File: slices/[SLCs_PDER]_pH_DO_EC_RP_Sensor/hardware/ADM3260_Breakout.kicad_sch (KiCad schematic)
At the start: 21 parts, among them J1 CONN_05LOCK_LONGPADS, J2 BNCPTH, Q1 BSS84, Q2 BSH105, Q3 BSS84, U1 ADM3260, U2 Atlas Scientific OEM pH or ORP

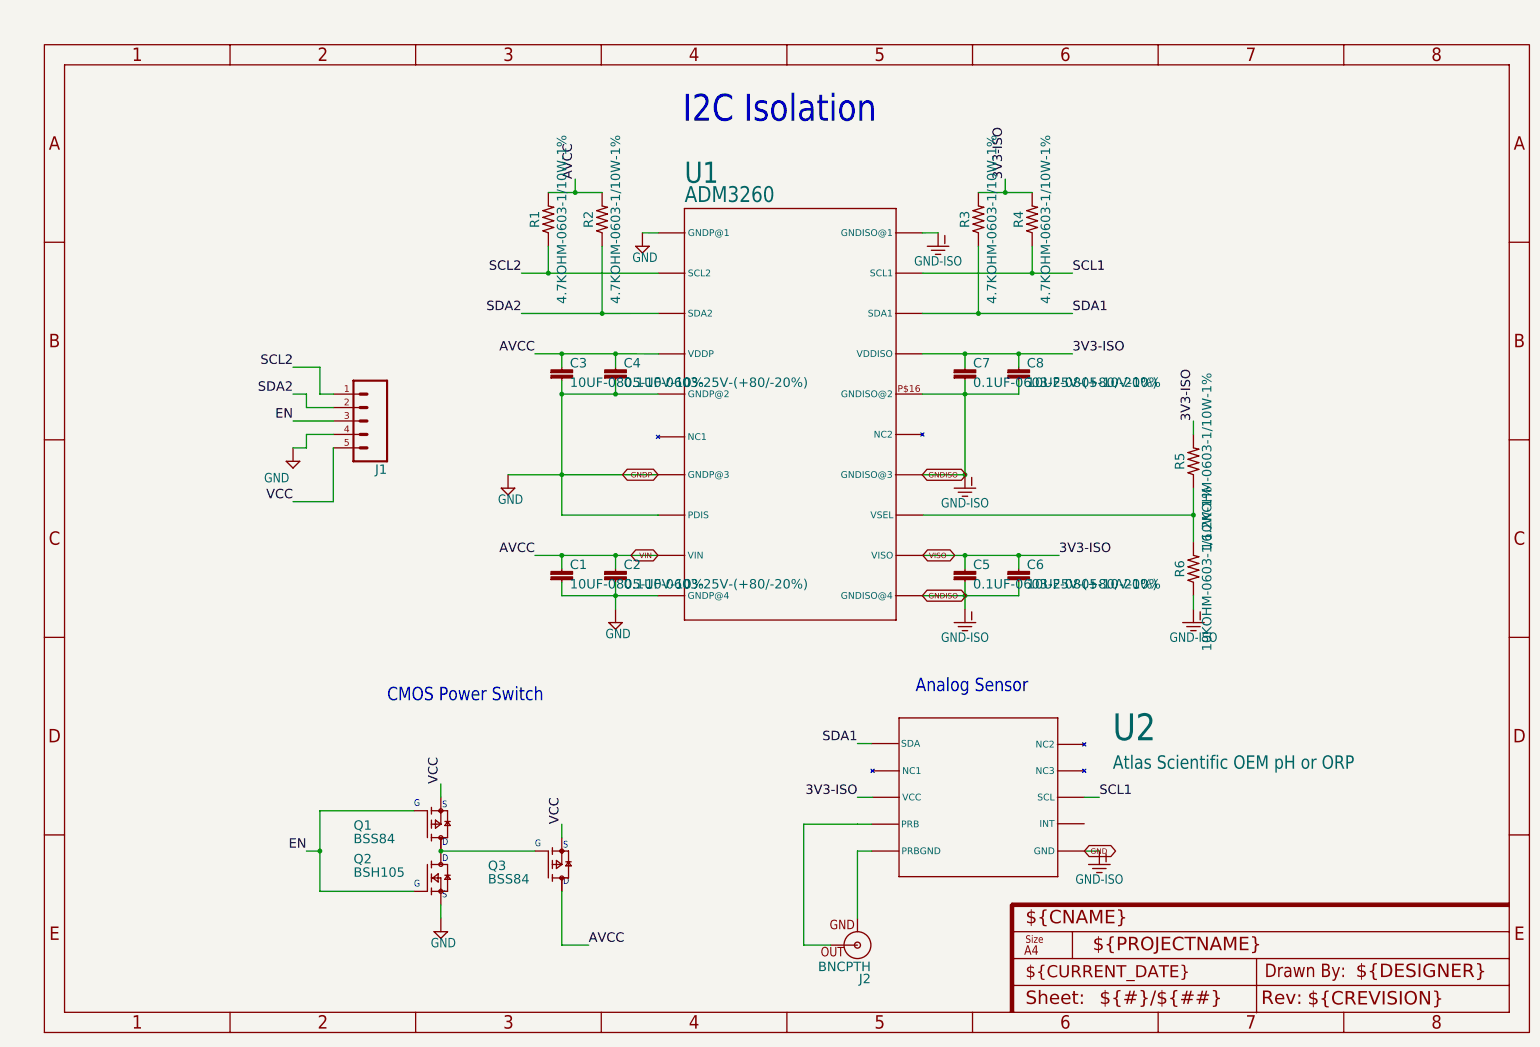
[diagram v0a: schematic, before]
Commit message: improved phdo and initial ERC pass on PDER
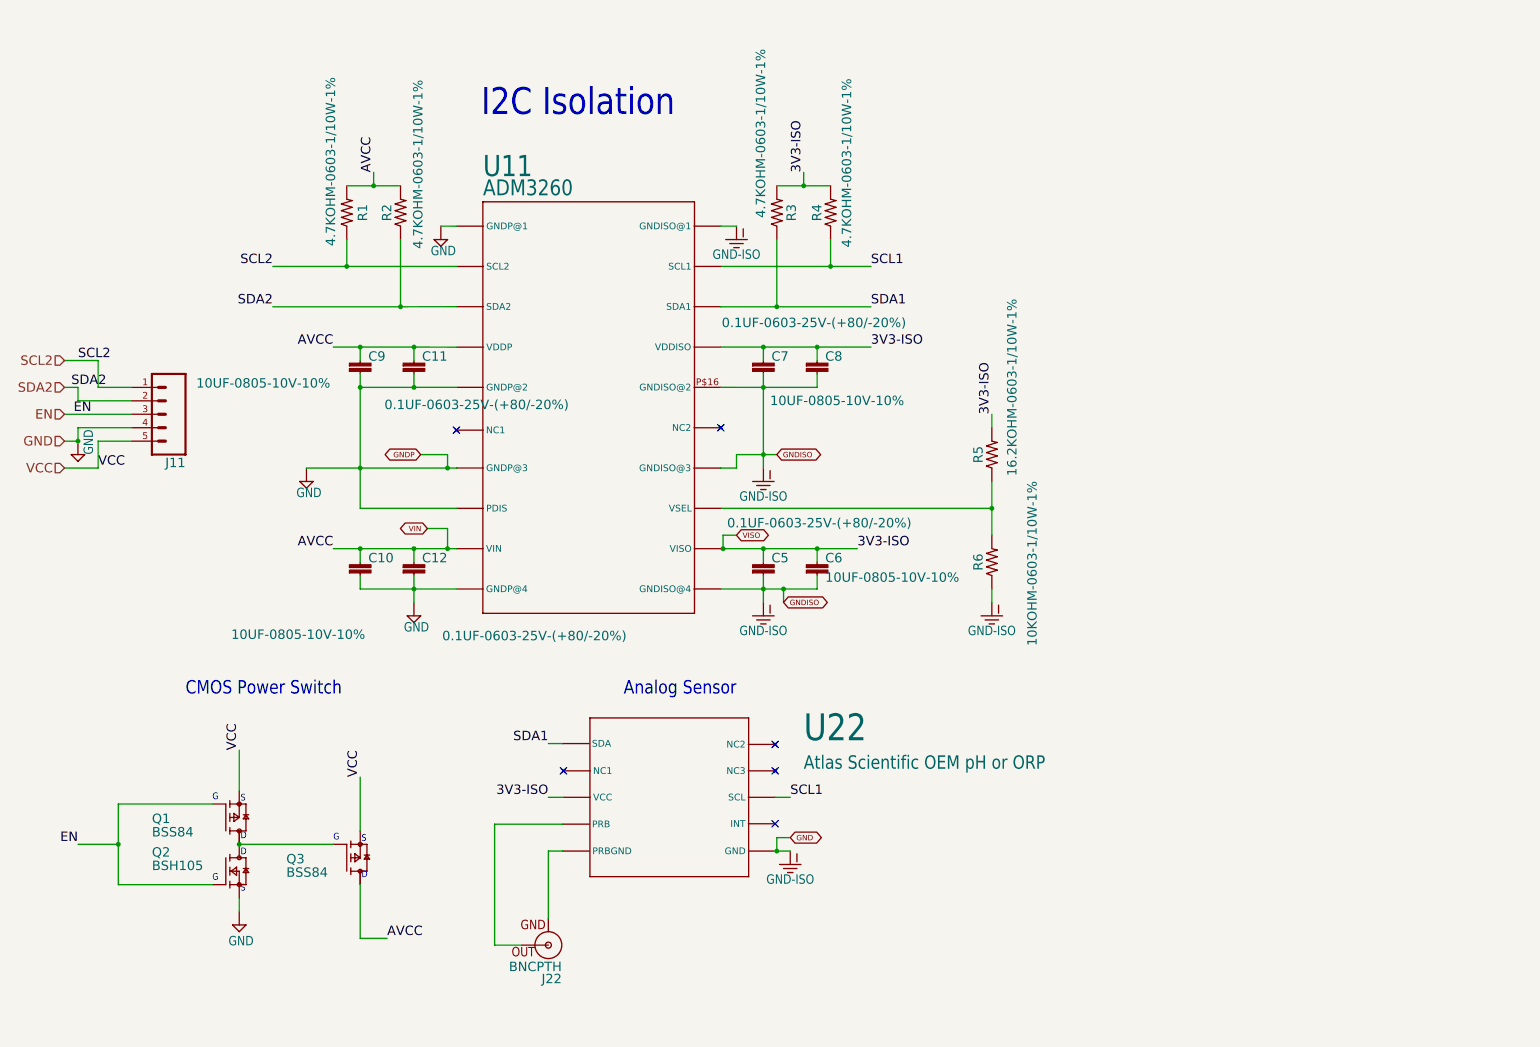
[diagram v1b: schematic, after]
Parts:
- C10: renamed from C1; footprint ADM3260_Breakout:0805 -> Capacitor_SMD:C_0805_2012Metric
- C11: renamed from C4; footprint ADM3260_Breakout:0603 -> Capacitor_SMD:C_0201_0603Metric
- C12: renamed from C2; footprint ADM3260_Breakout:0603 -> Capacitor_SMD:C_0201_0603Metric
- C5, C7: footprint ADM3260_Breakout:0603 -> Capacitor_SMD:C_0201_0603Metric
- C6, C8: footprint ADM3260_Breakout:0805 -> Capacitor_SMD:C_0805_2012Metric
- C9: renamed from C3; footprint ADM3260_Breakout:0805 -> Capacitor_SMD:C_0805_2012Metric
- J11: renamed from J1; footprint ADM3260_Breakout:1X05_LOCK_LONGPADS -> Connector_JST:JST_EH_B5B-EH-A_1x05_P2.50mm_Vertical
- J22: renamed from J2; footprint ADM3260_Breakout:BNC -> Connector_Coaxial:BNC_Amphenol_B6252HB-NPP3G-50_Horizontal
- Q1, Q2, Q3: footprint ADM3260_Breakout:SOT23 -> Package_TO_SOT_SMD:SOT-23-3
- R1, R2, R3, R4, R5, R6: footprint ADM3260_Breakout:0603 -> Resistor_SMD:R_0201_0603Metric
- renumbered U1 to U11, U2 to U22
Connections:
- net 3V3-ISO is gone; now on net VISO: C5.1, C6.1, C7.1, C8.1, R3.2, R4.2, R5.2, U11.P$17 (VDDISO), U22.P$3 (VCC)
- net AVCC is gone; now on net VIN: C10.1, C11.1, C12.1, C9.1, Q3.3 (D), R1.2, R2.2, U11.P$4 (VDDP)
- net GNDP is gone; now on net GND: U11.P$7 (GNDP@3)
- net GND: now also U11.P$8 (PDIS)
- net SDA1: now also U22.P$1 (SDA)
- net at J22.GND: now also U22.P$5 (PRBGND)
- net at J22.S (OUT): now also U22.P$4 (PRB)
- net at R5.1, R6.2: now also U11.P$13 (VSEL)
- no-connect marks 0 -> 6
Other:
- company: (none) -> FAST Research et al.
- title: (none) -> ADM3260 with Atlas Scientific OEM
- moved on the sheet: C10, C11, C12, C5, C6, C7, C8, C9, J11, J22, Q1, Q2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

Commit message: atlas oem slice footprints all done and at routing stage
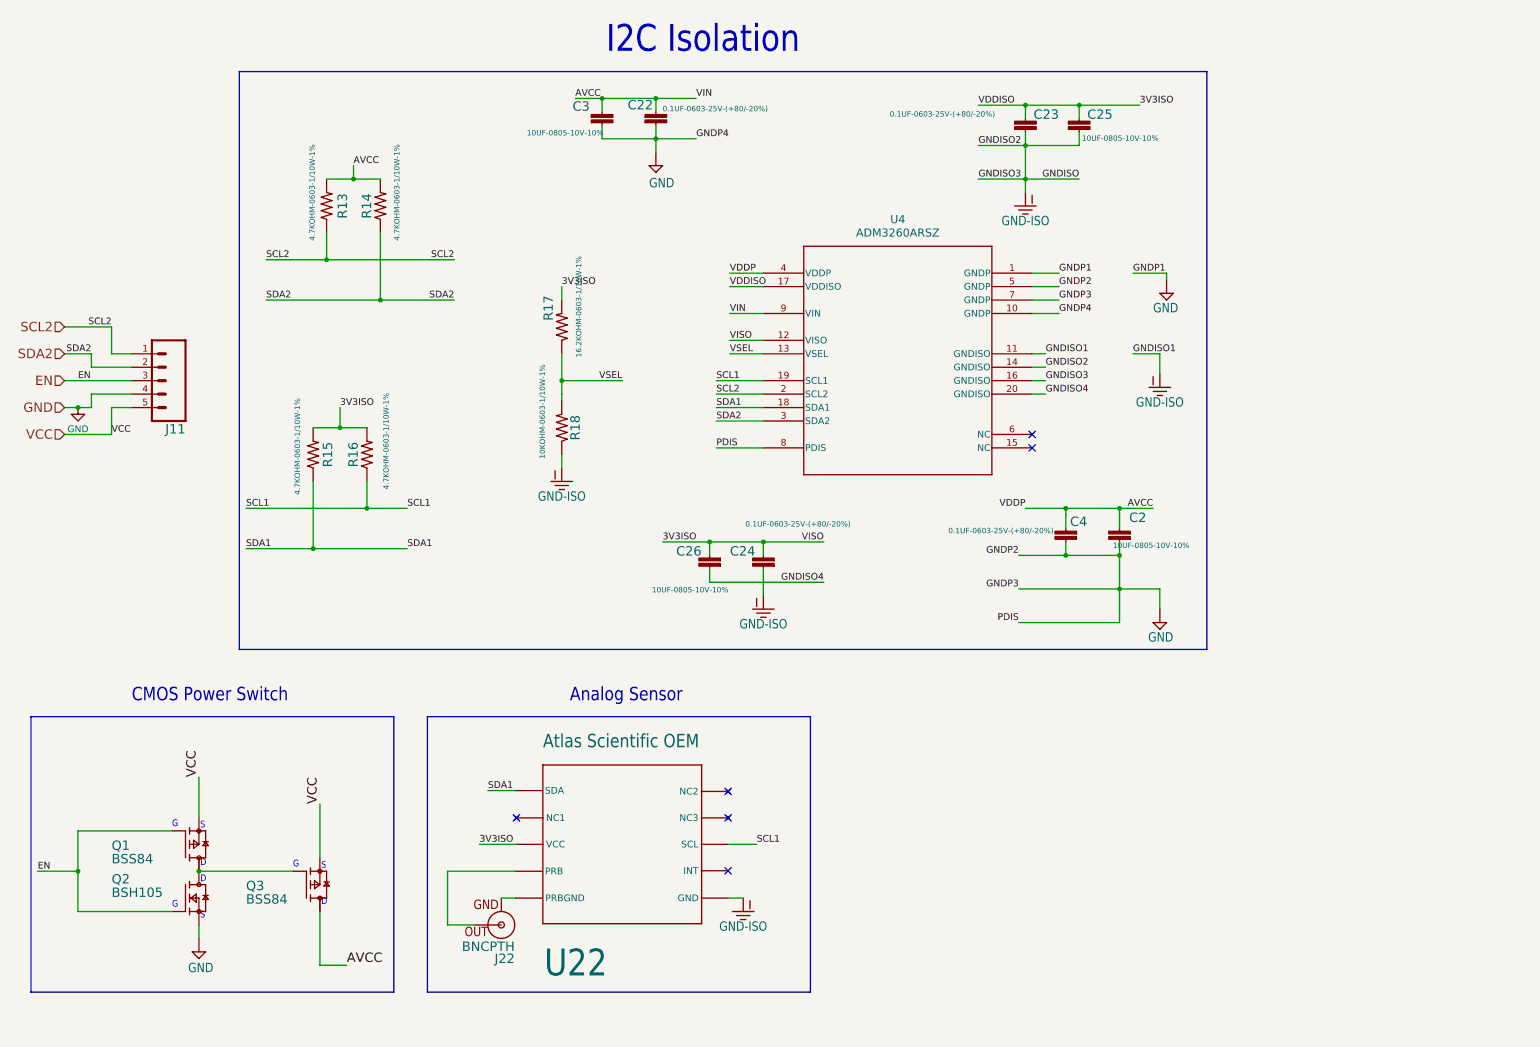
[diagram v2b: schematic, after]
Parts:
- removed C10, C6, C8, C9: 10UF-0805-10V-10%, Capacitor_SMD:C_0805_2012Metric, symbol ADM3260_Breakout-eagle-import:10UF-0805-10V-10%
- removed C11, C12, C5, C7: 0.1UF-0603-25V-(+80/-20%), Capacitor_SMD:C_0201_0603Metric, symbol ADM3260_Breakout-eagle-import:0.1UF-0603-25V-(+80/-20%)
- removed R1, R2, R3, R4: 4.7KOHM-0603-1/10W-1%, Resistor_SMD:R_0201_0603Metric, symbol ADM3260_Breakout-eagle-import:4.7KOHM-0603-1/10W-1%
- removed R5: 16.2KOHM-0603-1/10W-1%, Resistor_SMD:R_0201_0603Metric, symbol ADM3260_Breakout-eagle-import:16.2KOHM-0603-1/10W-1%
- removed R6: 10KOHM-0603-1/10W-1%, Resistor_SMD:R_0201_0603Metric, symbol ADM3260_Breakout-eagle-import:10KOHM-0603-1/10W-1%
- removed U11: ADM3260, ADM3260_Breakout:ADM3260, symbol ADM3260_Breakout-eagle-import:ADM3260
- added C2, C25, C26, C3: 10UF-0805-10V-10%, Capacitor_SMD:C_0805_2012Metric, symbol ADM3260_Breakout-eagle-import:10UF-0805-10V-10%
- added C22, C23, C24, C4: 0.1UF-0603-25V-(+80/-20%), Capacitor_SMD:C_0201_0603Metric, symbol ADM3260_Breakout-eagle-import:0.1UF-0603-25V-(+80/-20%)
- added R13, R14, R15, R16: 4.7KOHM-0603-1/10W-1%, Resistor_SMD:R_0201_0603Metric, symbol ADM3260_Breakout-eagle-import:4.7KOHM-0603-1/10W-1%
- added R17: 16.2KOHM-0603-1/10W-1%, Resistor_SMD:R_0201_0603Metric, symbol ADM3260_Breakout-eagle-import:16.2KOHM-0603-1/10W-1%
- added R18: 10KOHM-0603-1/10W-1%, Resistor_SMD:R_0201_0603Metric, symbol ADM3260_Breakout-eagle-import:10KOHM-0603-1/10W-1%
- added U4: ADM3260ARSZ, ADM3260ARSZ:RS_20_ADI, symbol ADM3260ARSZ:ADM3260ARSZ
- U22: value Atlas Scientific OEM pH or ORP -> Atlas Scientific OEM; footprint ADM3260_Breakout:PHSENSOR -> Atlas-Scientific:Atlas_OEM
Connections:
- net GND: now also C2.2, C22.2, C3.2, C4.2, U4.1 (GNDP), U4.10 (GNDP), U4.5 (GNDP), U4.7 (GNDP), U4.8 (PDIS); no longer U22.P$6 (GND)
- net SCL1: now also U22.P8 (SCL), R16.1, U4.19 (SCL1); no longer U22.P$8 (SCL)
- net SCL2: now also R13.1, U4.2 (SCL2)
- net SDA1: now also U22.P1 (SDA), R15.1, U4.18 (SDA1); no longer U22.P$1 (SDA)
- net SDA2: now also R14.1, U4.3 (SDA2)
- net at J22.GND: now also U22.P5 (PRBGND); no longer U22.P$5 (PRBGND)
- net at J22.S (OUT): now also U22.P4 (PRB); no longer U22.P$4 (PRB)
- net VIN renamed AVCC
- net AVCC: now also C2.1, C22.1, C3.1, C4.1, R13.2, R14.2, U4.4 (VDDP), U4.9 (VIN)
- removed net VISO: U22.P$3 (VCC)
- new net 3V3ISO: C23.1, C24.1, C25.1, C26.1, R15.2, R16.2, R17.2, U22.P3 (VCC), U4.12 (VISO), U4.17 (VDDISO)
- new net GND-ISO: C23.2, C24.2, C25.2, R18.1, U22.P6 (GND), U4.11 (GNDISO), U4.14 (GNDISO), U4.16 (GNDISO)
- new net GNDISO4: C26.2, U4.20 (GNDISO)
- new net VSEL: R17.1, R18.2, U4.13 (VSEL)
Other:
- moved on the sheet: J11, J22, Q1, Q2, Q3, U22
